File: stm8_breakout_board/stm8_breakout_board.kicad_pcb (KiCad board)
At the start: 2 copper layers, 21.4 x 26.5 mm, 23 parts, among them J1 STLinkV2 Connector, J2 Conn_01x10_Male, J3 Power Connector, J4 Conn_01x10_Male, SW1 Reset, U1 STM8S003F3P, U2 XC6206, U3 AMS1117-3.3

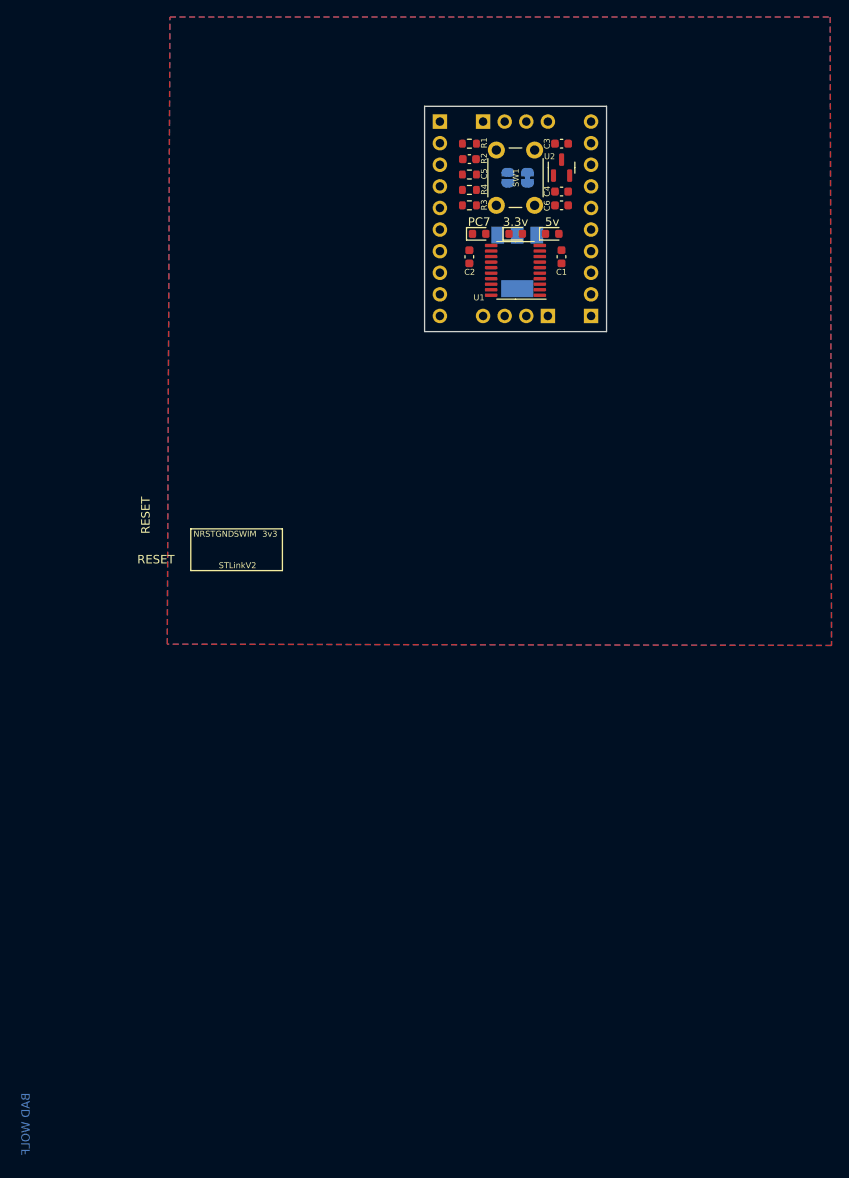
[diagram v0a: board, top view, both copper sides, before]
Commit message: as-ordered boards
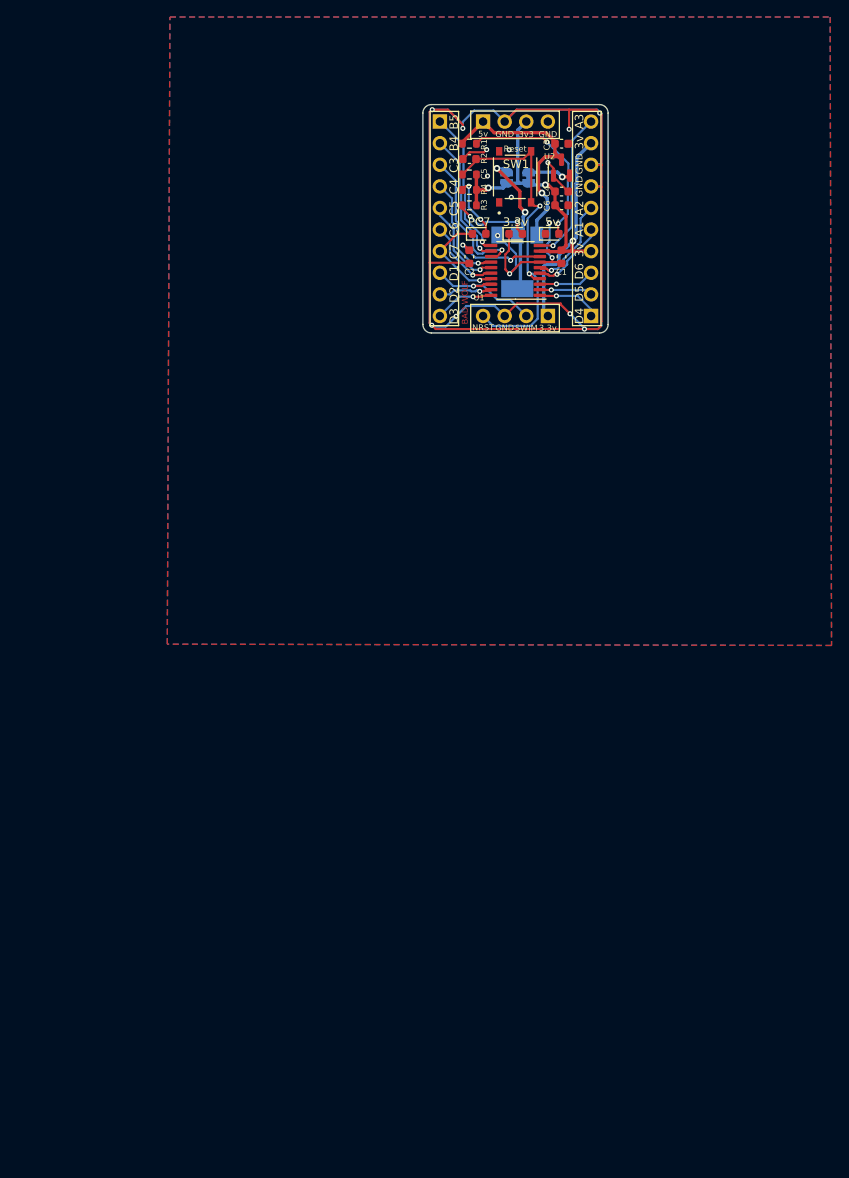
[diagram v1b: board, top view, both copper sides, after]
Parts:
- SW1: footprint Button_Switch_THT:SW_PUSH_6mm_H4.3mm -> custom_items:SW_TS-1187A-B-A-B
- moved SW1 4.01 mm to (108.8, 36.5)
- moved JP1 0.15 mm to (110.5, 36.6)
- moved JP2 0.15 mm to (107.8, 36.6)
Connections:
- J4 pad 1: PB4 -> PB5
- J4 pad 2: PB5 -> PB4
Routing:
- net GND: track 0.00 -> 227.7 mm, vias 0 -> 17
- net +3V3: track 0.00 -> 59.9 mm, vias 0 -> 3
- net NRST: track 0.00 -> 39.9 mm, vias 0 -> 2
- net +5V: track 0.00 -> 28.0 mm, vias 0 -> 1
- net Net-(D1-Pad2): track 0.00 -> 21.1 mm, vias 0 -> 2
- net PA3: track 0.00 -> 18.0 mm, vias 0 -> 1
- net Net-(JP2-Pad1): track 0.00 -> 17.6 mm, vias 0 -> 2
- net PB5: track 0.00 -> 17.5 mm, vias 0 -> 1
- net PC3: track 0.00 -> 17.0 mm, vias 0 -> 1
- net PB4: track 0.00 -> 15.8 mm, vias 0 -> 1
- net PD1: track 0.00 -> 14.5 mm, vias 0 -> 1
- net PC4: track 0.00 -> 12.9 mm, vias 0 -> 1
- net PC7: track 0.00 -> 12.2 mm, vias 0 -> 1
- net PC5: track 0.00 -> 11.1 mm, vias 0 -> 1
- net PA2: track 0.00 -> 11.1 mm, vias 0 -> 1
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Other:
- board size 21.4 x 26.5 mm -> 21.8 x 26.9 mm
- board text added: "3.3v"
- board text added: "3v"
- board text added: "5v"
- board text added: "A1"
- board text added: "A2"
- board text added: "A3"
- board text added: "B4"
- board text added: "B5"
- board text added: "C3"
- board text added: "C4"
- board text added: "C5"
- board text added: "C6"
- board text added: "C7"
- board text added: "D1"
- board text added: "D2"
- board text added: "D3"
- board text added: "D4"
- board text added: "D5"
- board text added: "D6"
- board text added: "STM8 Dev Board v1.0"
- board text added: "github.com/akuker/hw_projects"
- board text removed: "POW ENB Override"
- board text removed: "RESET"
- board text removed: "STLinkV2"
- board text removed: "SuperUPS for Raspberry Pi v0.9.5"
- board text removed: "https://github.com/akuker/SuperUPS"
